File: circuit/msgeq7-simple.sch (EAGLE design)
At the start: 30 parts, among them IC1 LM3915N, IC2 MSGEQ7, Q1 BS250, Q2 BS250, Q3 BS250, Q4 BS250, Q5 BS250, Q6 BS250, Q7 BS250, X1 KLBR4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

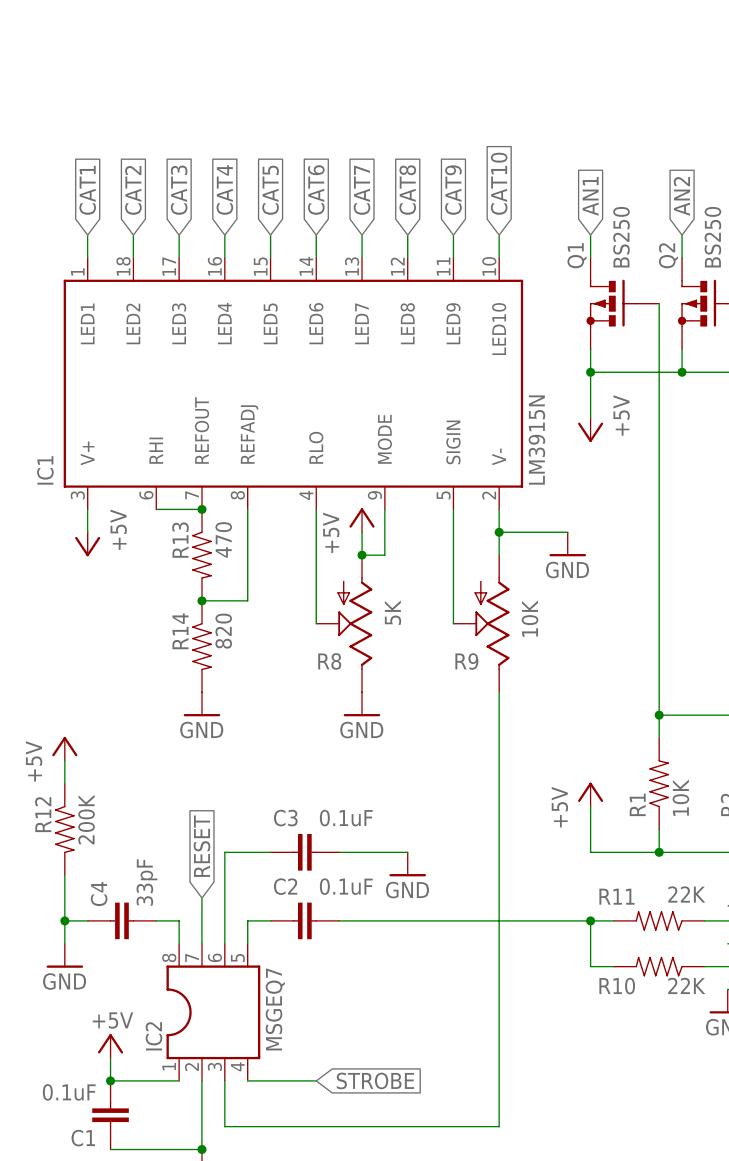
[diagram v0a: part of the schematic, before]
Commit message: fixed location of R12
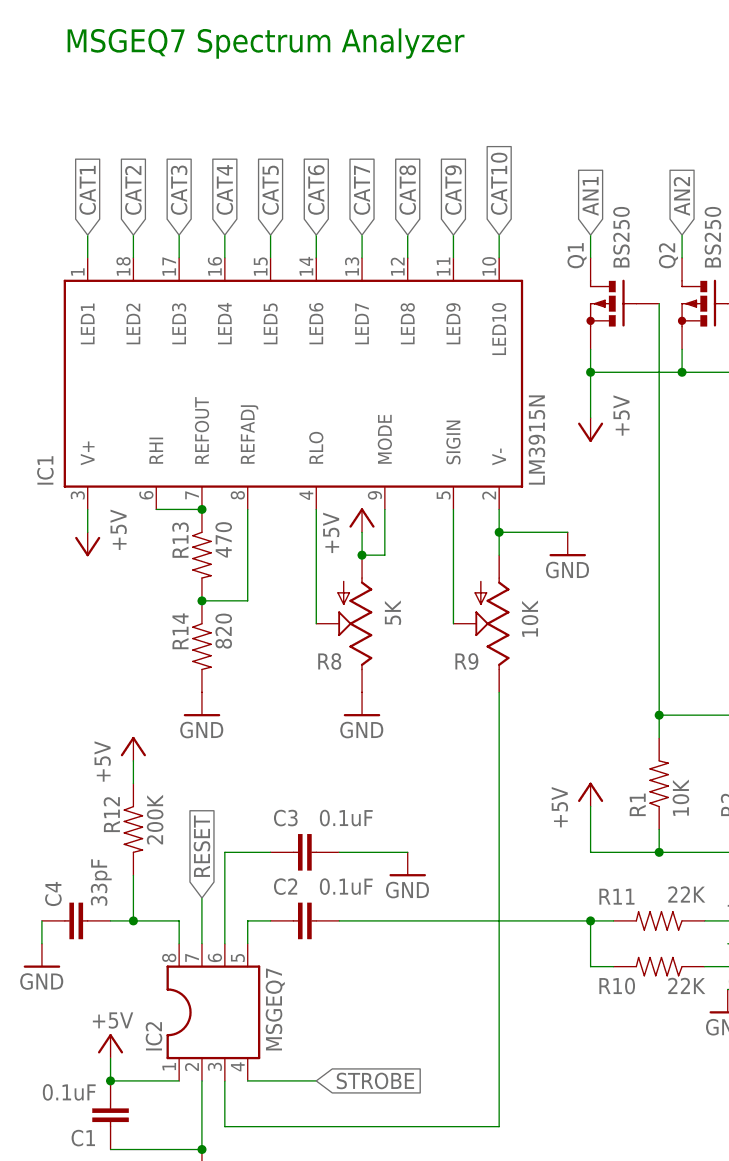
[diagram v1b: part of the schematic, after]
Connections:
- net GND: no longer R12.2
- net N$15: now also R12.2
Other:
- note added: "MSGEQ7 Spectrum Analyzer"
- moved on the sheet: C4, R12
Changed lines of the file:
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@@
 <setting verticaltext="up"/>
 </settings>
-<grid distance="0.1" unitdist="inch" unit="inch" style="lines" multiple="1" display="yes" altdistance="0.05" altunitdist="inch" altunit="inch"/>
+<grid distance="0.1" unitdist="inch" unit="inch" style="lines" multiple="1" display="yes" altdistance="0.01" altunitdist="inch" altunit="inch"/>
 <layers>
 <layer number="1" name="Top" color="4" fill="1" visible="no" active="no"/>
@@
 <part name="GND8" library="supply1" deviceset="GND" device=""/>
 <part name="P+7" library="supply1" deviceset="+5V" device=""/>
-<part name="FRAME1" library="frames" deviceset="A4L-LOC" device=""/>
 </parts>
 <sheets>
 <sheet>
 <plain>
+<text x="-15.24" y="99.06" size="2.54" layer="91">MSGEQ7 Spectrum Analyzer</text>
 </plain>
 <instances>
@@
 </instance>
 <instance part="GND6" gate="1" x="22.86" y="7.62"/>
-<instance part="C4" gate="G$1" x="-7.62" y="2.54" rot="R90"/>
-<instance part="R12" gate="G$1" x="-15.24" y="12.7" rot="MR270"/>
-<instance part="GND7" gate="1" x="-15.24" y="-2.54"/>
-<instance part="P+6" gate="1" x="-15.24" y="22.86"/>
+<instance part="C4" gate="G$1" x="-12.7" y="2.54" rot="R90"/>
+<instance part="R12" gate="G$1" x="-7.62" y="12.7" rot="MR270"/>
+<instance part="GND7" gate="1" x="-17.78" y="-2.54"/>
+<instance part="P+6" gate="1" x="-7.62" y="22.86"/>
 <instance part="R13" gate="G$1" x="0" y="43.18" rot="MR270"/>
 <instance part="R14" gate="G$1" x="0" y="33.02" rot="MR270"/>
 <instance part="GND8" gate="1" x="0" y="25.4"/>
 <instance part="P+7" gate="1" x="43.18" y="55.88" rot="R180"/>
-<instance part="FRAME1" gate="G$1" x="-55.88" y="-55.88"/>
 </instances>
 <busses>
@@
 <pinref part="P+6" gate="1" pin="+5V"/>
 <pinref part="R12" gate="G$1" pin="1"/>
-<wire x1="-15.24" y1="20.32" x2="-15.24" y2="17.78" width="0.1524" layer="91"/>
+<wire x1="-7.62" y1="20.32" x2="-7.62" y2="17.78" width="0.1524" layer="91"/>
 </segment>
 <segment>
@@
 </segment>
 <segment>
-<pinref part="R12" gate="G$1" pin="2"/>
-<wire x1="-15.24" y1="7.62" x2="-15.24" y2="2.54" width="0.1524" layer="91"/>
 <pinref part="C4" gate="G$1" pin="1"/>
-<wire x1="-15.24" y1="2.54" x2="-12.7" y2="2.54" width="0.1524" layer="91"/>
-<wire x1="-15.24" y1="2.54" x2="-15.24" y2="0" width="0.1524" layer="91"/>
-<junction x="-15.24" y="2.54"/>
+<wire x1="-17.78" y1="2.54" x2="-17.78" y2="0" width="0.1524" layer="91"/>
 <pinref part="GND7" gate="1" pin="GND"/>
 </segment>
@@
 <segment>
 <pinref part="C4" gate="G$1" pin="2"/>
-<wire x1="-5.08" y1="2.54" x2="-2.54" y2="2.54" width="0.1524" layer="91"/>
+<wire x1="-10.16" y1="2.54" x2="-7.62" y2="2.54" width="0.1524" layer="91"/>
 <pinref part="IC2" gate="G$1" pin="8"/>
+<wire x1="-7.62" y1="2.54" x2="-2.54" y2="2.54" width="0.1524" layer="91"/>
 <wire x1="-2.54" y1="2.54" x2="-2.54" y2="0" width="0.1524" layer="91"/>
-</segment>
-</net>
+<pinref part="R12" gate="G$1" pin="2"/>
+<wire x1="-7.62" y1="7.62" x2="-7.62" y2="2.54" width="0.1524" layer="91"/>
+<junction x="-7.62" y="2.54"/>
+</segment>
+</net>
